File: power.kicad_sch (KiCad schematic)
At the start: 34 parts, among them J1 Batt_conn_3p, J2 USB_C_Receptacle_PowerOnly_6P, J3 Conn_01x03_Pin, Q1 DTC143Z, U1 BQ24073RGTR, U2 TPD1E10B06DPYR, U3 TPD1E10B06DPYR, U4 TPD1E10B06DPYR, U5 TPS61022RWUR, U7 AP2112K-1.8

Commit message: Prepeared production files
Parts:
- U5: LCSC (none) -> C915088
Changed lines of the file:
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@@
 			)
 		)
-		(property "LCSC" ""
+		(property "LCSC" "C915088"
 			(at 175.26 71.12 0)
 			(effects

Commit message: Cleaned up libs
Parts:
- J1: footprint Muffin_CONNECTOR_THT:BATTERY_P2+P1.27mm_Horizontal -> Connector_Muffin_THT.pretty:BATTERY_P2+P1.27mm_Horizontal
- J3: footprint Muffin_CONNECTOR_THT:PinHeader_1x03_P2.54mm_Horizontal -> Connector_Muffin_THT.pretty:PinHeader_1x03_P2.54mm_Horizontal
- Q1: footprint SOT-523:SOT-523 -> Muffin_SMD:SOT-523
- U1: footprint BQ24703:RGT16_1P7X1P7 -> Muffin_SMD:RGT16; symbol BQ24073:BQ24073RGTR -> Muffin_PMIC:BQ24073RGTR
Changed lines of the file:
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@@
 	)
 	(symbol
-		(lib_id "BQ24073:BQ24073RGTR")
+		(lib_id "Muffin_PMIC:BQ24073RGTR")
 		(at 59.69 35.56 0)
 		(unit 1)
@@
 			)
 		)
-		(property "Footprint" "BQ24703:RGT16_1P7X1P7"
+		(property "Footprint" "Muffin_SMD:RGT16"
 			(at 59.69 35.56 0)
 			(effects
@@
 			)
 		)
-		(property "Footprint" "SOT-523:SOT-523"
+		(property "Footprint" "Muffin_SMD:SOT-523"
 			(at 273.05 73.66 0)
 			(effects
@@
 			)
 		)
-		(property "Footprint" "Muffin_CONNECTOR_THT:PinHeader_1x03_P2.54mm_Horizontal"
+		(property "Footprint" "Connector_Muffin_THT.pretty:PinHeader_1x03_P2.54mm_Horizontal"
 			(at 251.46 77.47 0)
 			(effects
@@
 			)
 		)
-		(property "Footprint" "Muffin_CONNECTOR_THT:BATTERY_P2+P1.27mm_Horizontal"
+		(property "Footprint" "Connector_Muffin_THT.pretty:BATTERY_P2+P1.27mm_Horizontal"
 			(at 101.6 116.84 0)
 			(effects

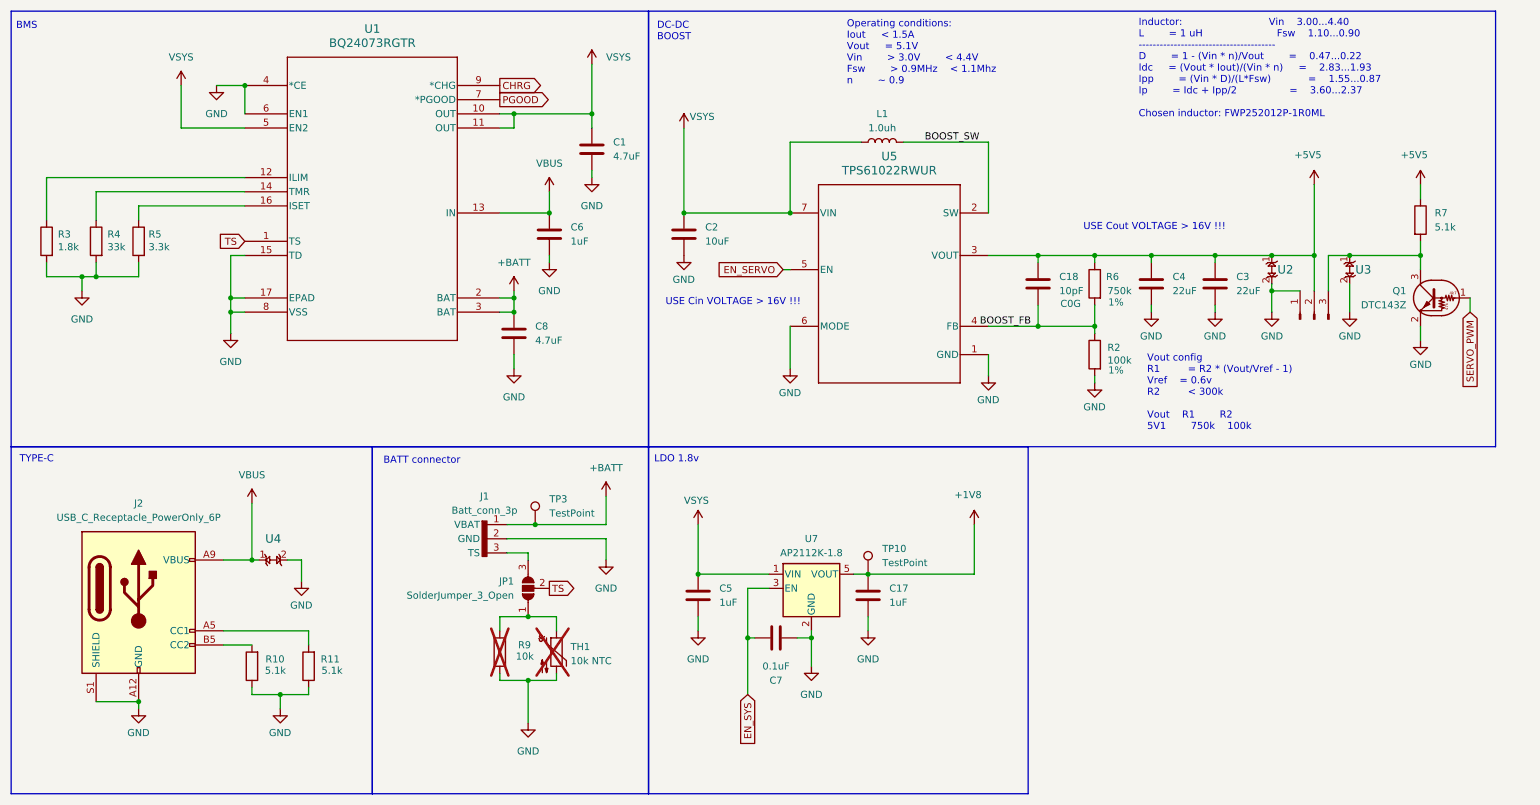
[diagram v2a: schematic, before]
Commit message: V4 revision - Moved usb to HID side - Changed battery connector to ph2.0 with standard(ish) pinout - Better footprints for debug and ldr connectors - Changed switch from SK12D07 to MSK12C02 - Changed R(ILIM) to 1.1k - Better placement of servo power and connector - Changed thermistor to 0402 SMD - Removed jumper to NTC
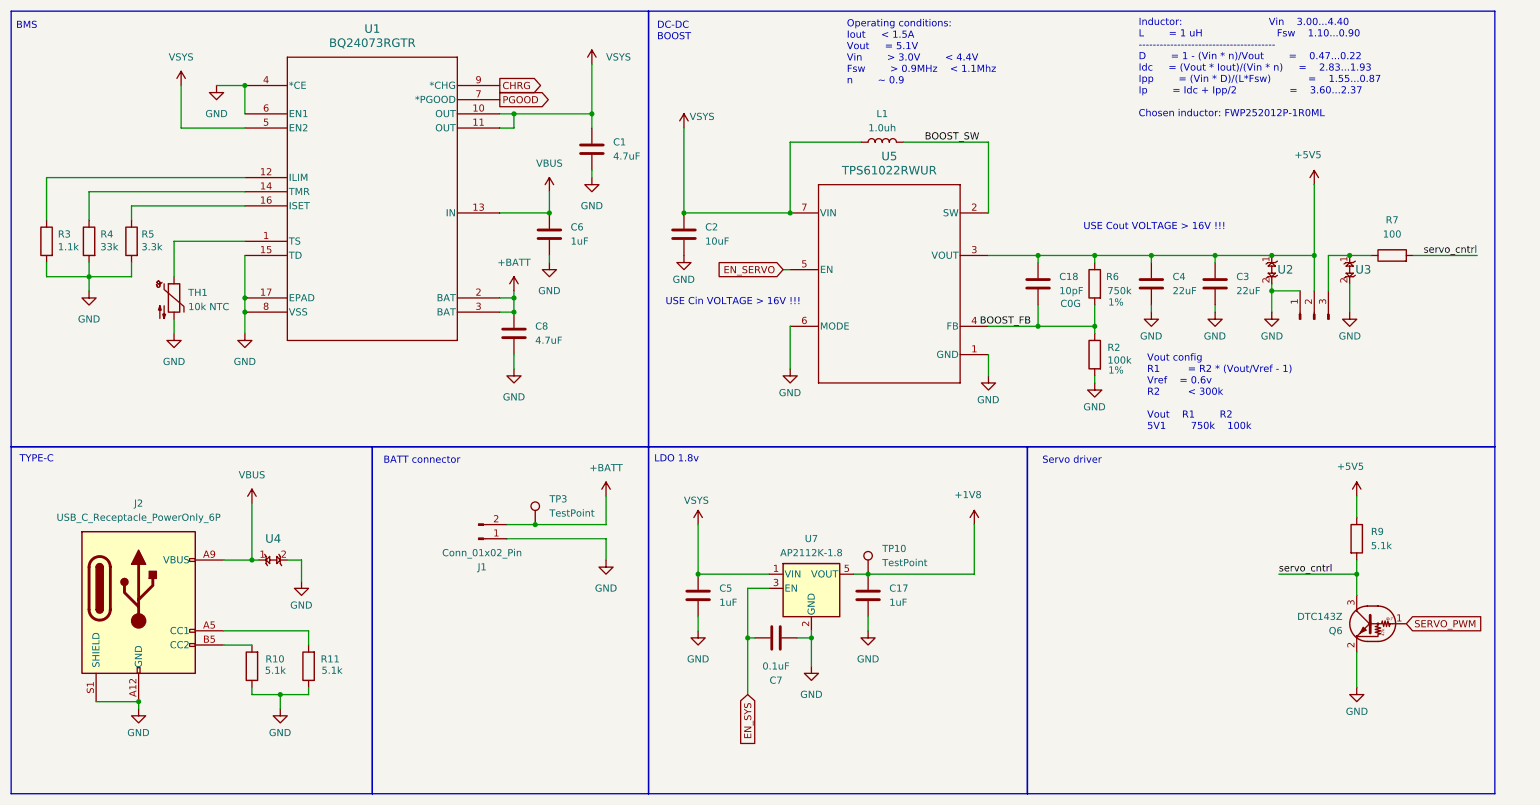
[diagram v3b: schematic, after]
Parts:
- removed J1: Batt_conn_3p, Connector_Muffin_THT.pretty:BATTERY_P2+P1.27mm_Horizontal, symbol Muffin_CONNECTORS:Batt_conn_3p
- removed JP1: SolderJumper_3_Open, Jumper:SolderJumper-3_P1.3mm_Open_RoundedPad1.0x1.5mm, symbol Jumper:SolderJumper_3_Open
- removed Q1: DTC143Z, Muffin_SMD:SOT-523, symbol Transistor_BJT:DTC143Z
- added J1: Conn_01x02_Pin, Connector_Muffin_THT.pretty:JST_PH_S2B-PH-K_1x02_P2.00mm_Horizontal, symbol Connector:Conn_01x02_Pin
- added Q6: DTC143Z, Muffin_SMD:SOT-523, symbol Transistor_BJT:DTC143Z
- R3: value 1.8k -> 1.1k
- R7: value 5.1k -> 100
- R9: value 10k -> 5.1k; now fitted
- TH1: footprint Resistor_THT:R_Axial_DIN0204_L3.6mm_D1.6mm_P1.90mm_Vertical -> Resistor_SMD:R_0402_1005Metric; now fitted
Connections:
- net TS is gone; now on an unnamed net: U1.1 (TS)
- net +5V5: now also R9.1; no longer R7.1
- net +BATT: now also J1.2 (Pin_2)
- net GND: now also J1.1 (Pin_1), Q6.2 (E); no longer R9.1
- net SERVO_PWM: now also Q6.1 (B)
- net at TH1.1: no longer R9.2
- net at J3.3 (Pin_3), U3.1: now also R7.1; no longer R7.2
- new net servo_cntrl: Q6.3 (C), R7.2, R9.2
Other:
- note added: "Servo driver"
- moved on the sheet: R4, R5, R7

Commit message: v4.1 - Changed SW2 to SMT (with lower profile) - Widen annular ring of vias - Small changes in routing (due to wider vias)
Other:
- moved on the sheet: J1, TP3
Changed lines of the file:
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@@
 	)
 	(junction
-		(at 111.76 114.3)
+		(at 106.68 118.11)
 		(diameter 0)
 		(color 0 0 0 0)
@@
 	(wire
 		(pts
-			(xy 124.46 114.3) (xy 111.76 114.3)
+			(xy 119.38 118.11) (xy 106.68 118.11)
 		)
 		(stroke
@@
 	(wire
 		(pts
-			(xy 124.46 116.84) (xy 124.46 120.65)
+			(xy 119.38 120.65) (xy 119.38 124.46)
 		)
 		(stroke
@@
 	(wire
 		(pts
-			(xy 124.46 109.22) (xy 124.46 114.3)
+			(xy 119.38 113.03) (xy 119.38 118.11)
 		)
 		(stroke
@@
 	(wire
 		(pts
-			(xy 106.68 116.84) (xy 124.46 116.84)
+			(xy 101.6 120.65) (xy 119.38 120.65)
 		)
 		(stroke
@@
 	(wire
 		(pts
-			(xy 111.76 114.3) (xy 106.68 114.3)
+			(xy 106.68 118.11) (xy 101.6 118.11)
 		)
 		(stroke
@@
 	(symbol
 		(lib_id "power:+BATT")
-		(at 124.46 109.22 0)
+		(at 119.38 113.03 0)
 		(unit 1)
 		(exclude_from_sim no)
@@
 		(fields_autoplaced yes)
 		(property "Reference" "#PWR021"
-			(at 124.46 113.03 0)
+			(at 119.38 116.84 0)
 			(effects
 				(font
@@
 		)
 		(property "Value" "+BATT"
-			(at 124.46 104.14 0)
+			(at 119.38 107.95 0)
 			(effects
 				(font
@@
 		)
 		(property "Footprint" ""
-			(at 124.46 109.22 0)
+			(at 119.38 113.03 0)
 			(effects
 				(font
@@
 		)
 		(property "Datasheet" ""
-			(at 124.46 109.22 0)
+			(at 119.38 113.03 0)
 			(effects
 				(font
@@
 		)
 		(property "Description" "Power symbol creates a global label with name \"+BATT\""
-			(at 124.46 109.22 0)
+			(at 119.38 113.03 0)
 			(effects
 				(font
@@
 	(symbol
 		(lib_id "Connector:TestPoint")
-		(at 111.76 114.3 0)
+		(at 106.68 118.11 0)
 		(unit 1)
 		(exclude_from_sim no)
@@
 		(fields_autoplaced yes)
 		(property "Reference" "TP3"
-			(at 114.3 109.7279 0)
+			(at 109.22 113.5379 0)
 			(effects
 				(font
@@
 		)
 		(property "Value" "TestPoint"
-			(at 114.3 112.2679 0)
+			(at 109.22 116.0779 0)
 			(effects
 				(font
@@
 		)
 		(property "Footprint" "TestPoint:TestPoint_Pad_D1.0mm"
-			(at 116.84 114.3 0)
+			(at 111.76 118.11 0)
 			(effects
 				(font
@@
 		)
 		(property "Datasheet" "~"
-			(at 116.84 114.3 0)
+			(at 111.76 118.11 0)
 			(effects
 				(font
@@
 		)
 		(property "Description" "test point"
-			(at 111.76 114.3 0)
+			(at 106.68 118.11 0)
 			(effects
 				(font
@@
 		)
 		(property "Tolerance " ""
-			(at 111.76 114.3 0)
+			(at 106.68 118.11 0)
 			(effects
 				(font
@@
 	(symbol
 		(lib_id "Connector:Conn_01x02_Pin")
-		(at 101.6 116.84 0)
+		(at 96.52 120.65 0)
 		(mirror x)
 		(unit 1)
@@
 		(dnp no)
 		(property "Reference" "J1"
-			(at 102.235 121.92 0)
+			(at 97.155 125.73 0)
 			(effects
 				(font
@@
 		)
 		(property "Value" "Conn_01x02_Pin"
-			(at 102.235 119.38 0)
+			(at 97.155 123.19 0)
 			(effects
 				(font
@@
 		)
 		(property "Footprint" "Connector_Muffin_THT.pretty:JST_PH_S2B-PH-K_1x02_P2.00mm_Horizontal"
-			(at 101.6 116.84 0)
+			(at 96.52 120.65 0)
 			(effects
 				(font
@@
 		)
 		(property "Datasheet" "~"
-			(at 101.6 116.84 0)
+			(at 96.52 120.65 0)
 			(effects
 				(font
@@
 		)
 		(property "Description" "Generic connector, single row, 01x02, script generated"
-			(at 101.6 116.84 0)
+			(at 96.52 120.65 0)
 			(effects
 				(font
@@
 	(symbol
 		(lib_id "power:GND")
-		(at 124.46 120.65 0)
+		(at 119.38 124.46 0)
 		(mirror y)
 		(unit 1)
@@
 		(fields_autoplaced yes)
 		(property "Reference" "#PWR022"
-			(at 124.46 127 0)
+			(at 119.38 130.81 0)
 			(effects
 				(font
@@
 		)
 		(property "Value" "GND"
-			(at 124.46 125.73 0)
+			(at 119.38 129.54 0)
 			(effects
 				(font
@@
 		)
 		(property "Footprint" ""
-			(at 124.46 120.65 0)
+			(at 119.38 124.46 0)
 			(effects
 				(font
@@
 		)
 		(property "Datasheet" ""
-			(at 124.46 120.65 0)
+			(at 119.38 124.46 0)
 			(effects
 				(font
@@
 		)
 		(property "Description" "Power symbol creates a global label with name \"GND\" , ground"
-			(at 124.46 120.65 0)
+			(at 119.38 124.46 0)
 			(effects
 				(font

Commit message: v4.3 - Smaller, faster, stronger (lol) - Removed few appendixes - Updated doc jobs set
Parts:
- TP3: value TestPoint -> VBAT
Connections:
- net servo_cntrl: now also J3.3 (Pin_3), R7.1, U3.1; no longer Q6.3 (C), R7.2, R9.2
- new net: Q6.3 (C), R7.2, R9.2
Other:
- moved on the sheet: R7, U3
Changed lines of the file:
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@@
 		(title "DRP.004")
 		(date "2025-04-05")
-		(rev "v4")
+		(rev "v4.3")
 		(company "SaintCarbonara")
 		(comment 1 "QUACK-QUACK, MAFAKA!")
@@
 	)
 	(junction
-		(at 257.81 66.04)
-		(diameter 0)
-		(color 0 0 0 0)
-	)
-	(junction
 		(at 157.48 58.42)
 		(diameter 0)
@@
 	(wire
 		(pts
-			(xy 245.11 123.19) (xy 259.08 123.19)
+			(xy 226.06 123.19) (xy 241.3 123.19)
 		)
 		(stroke
@@
 	(wire
 		(pts
+			(xy 248.92 123.19) (xy 259.08 123.19)
+		)
+		(stroke
+			(width 0)
+			(type default)
+		)
+	)
+	(wire
+		(pts
 			(xy 193.04 66.04) (xy 201.93 66.04)
 		)
@@
 	(wire
 		(pts
-			(xy 254 66.04) (xy 257.81 66.04)
+			(xy 254 66.04) (xy 265.43 66.04)
 		)
 		(stroke
@@
 	(wire
 		(pts
-			(xy 257.81 71.12) (xy 257.81 76.2)
+			(xy 270.51 66.04) (xy 270.51 74.93)
 		)
 		(stroke
@@
 	(wire
 		(pts
-			(xy 280.67 66.04) (xy 269.24 66.04)
-		)
-		(stroke
-			(width 0)
-			(type default)
-		)
-	)
-	(wire
-		(pts
 			(xy 168.91 123.19) (xy 171.45 123.19)
 		)
@@
 	(wire
 		(pts
-			(xy 257.81 66.04) (xy 261.62 66.04)
-		)
-		(stroke
-			(width 0)
-			(type default)
-		)
-	)
-	(wire
-		(pts
 			(xy 233.68 74.93) (xy 233.68 76.2)
 		)
@@
 	)
 	(label "servo_cntrl"
-		(at 280.67 66.04 180)
+		(at 254 66.04 0)
 		(effects
 			(font
 				(size 1.27 1.27)
 			)
-			(justify right bottom)
+			(justify left bottom)
 		)
 	)
 	(label "servo_cntrl"
-		(at 245.11 123.19 0)
+		(at 226.06 123.19 0)
 		(effects
 			(font
@@
 	(symbol
 		(lib_id "power:GND")
-		(at 257.81 76.2 0)
+		(at 270.51 74.93 0)
 		(unit 1)
 		(exclude_from_sim no)
@@
 		(dnp no)
 		(property "Reference" "#PWR027"
-			(at 257.81 82.55 0)
+			(at 270.51 81.28 0)
 			(effects
 				(font
@@
 		)
 		(property "Value" "GND"
-			(at 259.842 80.518 0)
+			(at 272.542 79.248 0)
 			(effects
 				(font
@@
 		)
 		(property "Footprint" ""
-			(at 257.81 76.2 0)
+			(at 270.51 74.93 0)
 			(effects
 				(font
@@
 		)
 		(property "Datasheet" ""
-			(at 257.81 76.2 0)
+			(at 270.51 74.93 0)
 			(effects
 				(font
@@
 		)
 		(property "Description" "Power symbol creates a global label with name \"GND\" , ground"
-			(at 257.81 76.2 0)
+			(at 270.51 74.93 0)
 			(effects
 				(font
@@
 	(symbol
 		(lib_id "Device:R")
-		(at 265.43 66.04 90)
+		(at 245.11 123.19 90)
 		(unit 1)
 		(exclude_from_sim no)
@@
 		(dnp no)
 		(property "Reference" "R7"
-			(at 265.43 59.69 90)
+			(at 245.11 116.84 90)
 			(effects
 				(font
@@
 		)
 		(property "Value" "100"
-			(at 265.43 62.23 90)
+			(at 245.11 119.38 90)
 			(effects
 				(font
@@
 		)
 		(property "Footprint" "Resistor_SMD:R_0603_1608Metric"
-			(at 265.43 67.818 90)
+			(at 245.11 124.968 90)
 			(effects
 				(font
@@
 		)
 		(property "Datasheet" "~"
-			(at 265.43 66.04 0)
+			(at 245.11 123.19 0)
 			(effects
 				(font
@@
 		)
 		(property "Description" "Resistor"
-			(at 265.43 66.04 0)
+			(at 245.11 123.19 0)
 			(effects
 				(font
@@
 	(symbol
 		(lib_id "Muffin_DIODES:TPD1E10B06DPYR")
-		(at 257.81 54.61 270)
+		(at 254 66.04 0)
 		(unit 1)
 		(exclude_from_sim no)
@@
 		(on_board yes)
 		(dnp no)
+		(fields_autoplaced yes)
 		(property "Reference" "U3"
-			(at 258.826 68.58 90)
+			(at 267.97 62.23 0)
 			(effects
 				(font
 					(size 1.524 1.524)
 				)
-				(justify left)
 			)
 		)
 		(property "Value" "TPD1E10B06DPYR"
-			(at 262.255 69.215 0)
+			(at 268.605 61.595 0)
 			(effects
 				(font
@@
 		)
 		(property "Footprint" "Muffin_SMD:X1SON-2_L1.0-W0.6-P0.65-BI"
-			(at 253.746 68.326 0)
+			(at 267.716 70.104 0)
 			(effects
 				(font
@@
 		)
 		(property "Datasheet" "TPD1E10B06DPYR"
-			(at 255.778 69.088 0)
+			(at 268.478 68.072 0)
 			(effects
 				(font
@@
 		)
 		(property "Description" ""
-			(at 257.81 54.61 0)
+			(at 254 66.04 0)
 			(effects
 				(font
@@
 		)
 		(property "LCSC" "C48260"
-			(at 251.46 68.072 0)
+			(at 267.462 72.39 0)
 			(effects
 				(font
@@
 			)
 		)
-		(property "Value" "TestPoint"
+		(property "Value" "VBAT"
 			(at 109.22 116.0779 0)
 			(effects

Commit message: Updated release project to new flow
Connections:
- net GND: now also J2.SH (SHIELD); no longer J2.S1 (SHIELD)
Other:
- moved on the sheet: U2, U3, U4
